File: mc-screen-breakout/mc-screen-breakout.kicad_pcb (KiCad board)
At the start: 4 copper layers, 32 x 20 mm, 29 parts, among them J1 USB_C_Receptacle_PowerOnly_6P, J2 FH28-10S-0.5SH_05_, SW1 NANOT160BP, SW2 NANOT160BP, U1 CMM-3424DT-26165-TR, U2 MDBT50Q-1MV2, Y1 32.768kHz

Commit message: Began drawing traces
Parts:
- removed the G*** at (37.5, 27.5)
- C1, C13, C2, C5, C8, C9: moved to F.Cu
- moved C13 20.4 mm to (60.2, 18.2), turned to 180 degrees
- moved U1 19.7 mm to (60.4, 20.6)
- moved C2 4.12 mm to (56.0, 24.0), turned to 0 degrees
- moved C5 3.75 mm to (53.5, 20.2)
- moved C1 3.17 mm to (56.0, 21.5), turned to 180 degrees
- moved C8 2.98 mm to (55.0, 18.8)
- moved C9 2.66 mm to (55.0, 17.2)
- moved L1 1.03 mm to (53.0, 18.2), turned to -90 degrees
- moved Y1 1.00 mm to (53.5, 22.8)
- moved C10 0.27 mm to (52.5, 28.1)
- moved C12 0.27 mm to (53.0, 26.1)
- moved J2 0.27 mm to (51.7, 30.5)
- moved C11 0.27 mm to (53.0, 27.1)
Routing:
- net GND: track 0.00 -> 39.5 mm, vias 0 -> 6
- net Net-(U2-SWDCLK): track 0.00 -> 17.1 mm, vias 0 -> 2
- net Net-(U2-SWDIO): track 0.00 -> 15.8 mm, vias 0 -> 2
- net VDD: track 0.00 -> 15.2 mm, vias 0 -> 3
- net MIC_SELECT: track 0.00 -> 8.93 mm, vias 0 -> 2
- net +BATT: track 0.00 -> 7.81 mm
- net Net-(U2-P0.01): track 0.00 -> 5.00 mm
- net Net-(U2-P0.00): track 0.00 -> 4.75 mm
- net LCD_DISP: track 0.00 -> 2.79 mm, vias 0 -> 1
- net Net-(U2-DCCH): track 0.00 -> 2.17 mm
- net MIC_DATA: track 0.00 -> 1.28 mm, vias 0 -> 1
- net MIC_CLK: track 0.00 -> 1.28 mm, vias 0 -> 1

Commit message: More routing
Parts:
- moved D2 0.17 mm to (58.0, 28.0)
- moved D3 0.08 mm to (59.8, 31.0)
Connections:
- C3 pad 1: +BATT -> Net-(D3-A1)
- D1 pad 2: Net-(D1-A2) -> GND
- D2 pad 2: Net-(D2-A2) -> GND
- D3 pad 2: +BATT -> GND
- R1 pad 1: Net-(D1-A2) -> Net-(D1-A1)
- R2 pad 2: Net-(D2-A2) -> Net-(D2-A1)
- U2 pad 13: unconnected-(U2-P0.28-Pad13) -> LCD_DISP
- U2 pad 14: unconnected-(U2-P0.30-Pad14) -> LCD_EXCOMIN
- U2 pad 16: LCD_DISP -> unconnected-(U2-P0.27-Pad16)
- U2 pad 19: LCD_EXCOMIN -> unconnected-(U2-P0.26-Pad19)
- U2 pad 20: unconnected-(U2-P0.04-Pad20) -> MIC_CLK
- U2 pad 21: unconnected-(U2-P0.05-Pad21) -> MIC_DATA
- U2 pad 22: unconnected-(U2-P0.06-Pad22) -> MIC_SELECT
- U2 pad 4: unconnected-(U2-P1.11-Pad4) -> LCD_SCK
- U2 pad 42: MIC_SELECT -> unconnected-(U2-P0.19-Pad42)
- U2 pad 43: MIC_CLK -> unconnected-(U2-P0.21-Pad43)
- U2 pad 44: MIC_DATA -> unconnected-(U2-P0.20-Pad44)
- U2 pad 45: LCD_SCK -> unconnected-(U2-P0.23-Pad45)
- U2 pad 48: LCD_SI -> unconnected-(U2-P0.24-Pad48)
- U2 pad 49: LCD_CS -> unconnected-(U2-P0.25-Pad49)
- U2 pad 6: unconnected-(U2-P1.13-Pad6) -> LCD_SI
- U2 pad 8: unconnected-(U2-P1.15-Pad8) -> LCD_CS
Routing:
- net MIC_DATA: track 1.28 -> 15.5 mm, vias 1 -> 2
- net MIC_CLK: track 1.28 -> 9.03 mm, vias 1 -> 2
- net LCD_SCK: track 0.00 -> 7.35 mm
- net LCD_SI: track 0.00 -> 7.19 mm
- net LCD_CS: track 0.00 -> 7.05 mm
- net LCD_DISP: track 2.79 -> 9.06 mm, vias 1 -> 2
- net LCD_EXCOMIN: track 0.00 -> 4.90 mm
- net MIC_SELECT: track 8.93 -> 9.75 mm
- net GND: track 39.5 -> 38.8 mm

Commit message: Initial routing almost done
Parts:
- C10, C11, C12, C3, D1, D2, D3, R1, R2: moved to F.Cu
- moved D3 17.0 mm to (43.0, 28.2)
- moved D2 15.5 mm to (43.0, 32.0)
- moved D1 15.1 mm to (43.0, 30.8)
- moved C3 15.1 mm to (43.0, 27.0)
- moved R2 14.0 mm to (43.0, 33.2)
- moved R1 13.0 mm to (43.0, 29.5)
- moved C12 5.77 mm to (47.2, 26.8), turned to 180 degrees
- moved C10 2.71 mm to (53.2, 25.5)
- moved C11 2.56 mm to (55.5, 26.8)
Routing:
- net Net-(D2-A1): track 0.00 -> 22.7 mm
- net Net-(D3-A1): track 0.00 -> 21.9 mm
- net Net-(D1-A1): track 0.00 -> 17.2 mm
- net GND: track 38.8 -> 49.9 mm, vias 6 -> 8
- net LCD_DISP: track 9.06 -> 12.1 mm, vias 2 -> 3
- net +BATT: track 7.81 -> 10.3 mm
- net VDD: track 15.2 -> 17.5 mm, vias 3 -> 4

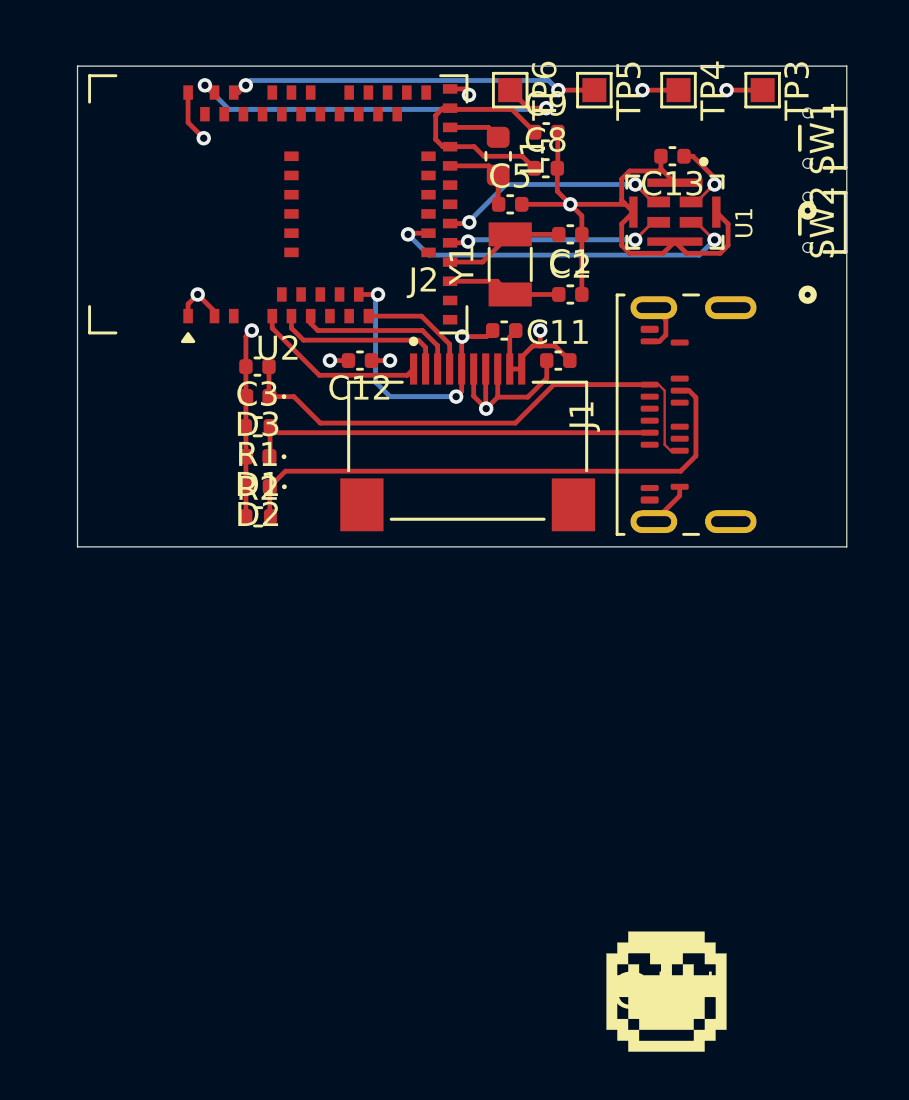
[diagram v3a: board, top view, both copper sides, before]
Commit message: Fixed DRC errors/warnings
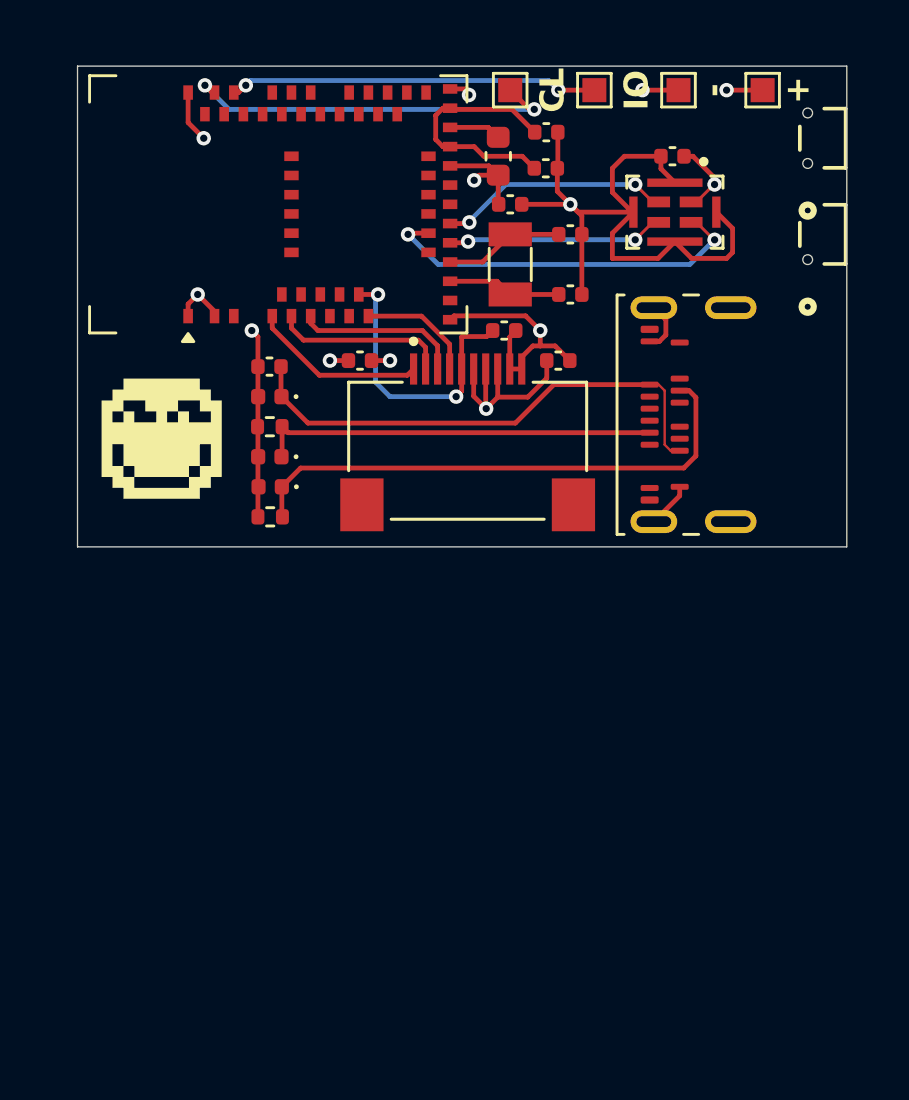
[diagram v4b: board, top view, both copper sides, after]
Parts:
- moved G*** 31.1 mm to (39.0, 30.0)
- moved C3 0.50 mm to (43.5, 27.0)
- moved D1 0.50 mm to (43.5, 30.8)
- moved D2 0.50 mm to (43.5, 32.0)
- moved D3 0.50 mm to (43.5, 28.2)
- moved R1 0.50 mm to (43.5, 29.5)
- moved R2 0.50 mm to (43.5, 33.2)
- moved SW2 0.50 mm to (66.5, 21.5)
- renumbered TP3 to +, TP4 to -, TP6 to CL, TP5 to IO
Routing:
- net GND: track 49.9 -> 57.1 mm
- net Net-(U2-SWDCLK): track 17.1 -> 16.1 mm
- net VDD: track 17.5 -> 18.4 mm, vias 4 -> 5
- net Net-(D3-A1): track 21.9 -> 21.4 mm
- net Net-(D2-A1): track 22.7 -> 22.2 mm
- net Net-(D1-A1): track 17.2 -> 16.7 mm
- net LCD_DISP: vias 3 -> 2
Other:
- board text added: "sugo14/Watch v1.0 28/07/2026"

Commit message: Drew custom switch footprint
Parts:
- SW1, SW2: footprint NANOT160BP:SW_NANOT160BP_CNK -> NANOT160BP:Untitled
- moved SW2 0.25 mm to (66.5, 21.8)
- moved SW1 0.20 mm to (66.7, 17.5)
- renumbered + to TP3, - to TP4, IO to TP5, CL to TP6
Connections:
- U2 pad 16: unconnected-(U2-P0.27-Pad16) -> SW2
- U2 pad 25: unconnected-(U2-P1.08-Pad25) -> SW1
- U2 pad 36: SW2 -> unconnected-(U2-P0.14-Pad36)
- U2 pad 37: SW1 -> unconnected-(U2-P0.13-Pad37)
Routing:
- net SW1: track 0.00 -> 19.3 mm, vias 0 -> 1
- net SW2: track 0.00 -> 18.1 mm, vias 0 -> 1
